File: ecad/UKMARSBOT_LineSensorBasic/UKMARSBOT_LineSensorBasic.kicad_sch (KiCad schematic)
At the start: 32 parts, among them J1 Conn_01x16, Q1 BC337-40, Q2 BPW85C, Q3 BPW85C, Q4 BPW85C, Q5 BPW85C, Q6 BC337-40

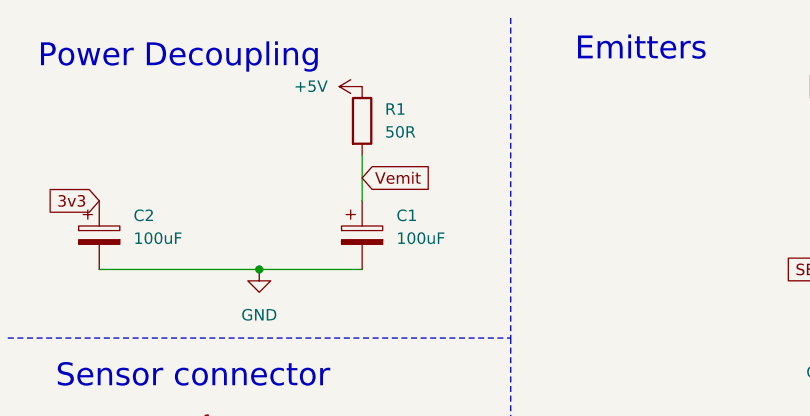
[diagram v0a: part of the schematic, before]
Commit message: Added RAPID field to all files and updated automation to pull this new field into BOM files
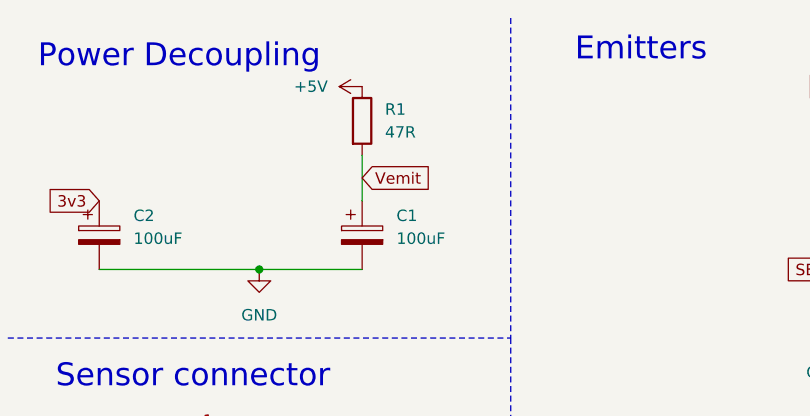
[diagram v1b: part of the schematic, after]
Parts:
- C1, C2: RAPID (none) -> 11-4109
- D1, D2, D7: RAPID (none) -> 55-0066
- D4: RAPID (none) -> 56-0400
- D5: RAPID (none) -> 56-0405
- D6: RAPID (none) -> 56-0410
- J1: RAPID (none) -> 19-0087
- Q1, Q6: RAPID (none) -> 50-3113
- R1: value 50R -> 47R; RAPID (none) -> 62-0334; RSONLINE (none) -> 707-8817
- R10, R11, R12, R14, R7, R8, R9: RAPID (none) -> 64-0068
- R15, R2: RAPID (none) -> 62-0360
- R16, R4: RAPID (none) -> 62-0394
- R17, R3, R5: RAPID (none) -> 62-0326

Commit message: V2.1 Boards ready for fabrication
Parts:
- C1, C2: footprint Capacitor_THT:CP_Radial_D5.0mm_P2.50mm -> Capacitor_THT:CP_Radial_D6.3mm_P2.50mm; RSONLINE 739-6799 -> 176-3779
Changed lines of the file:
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@@
 			)
 		)
-		(property "Footprint" "Capacitor_THT:CP_Radial_D5.0mm_P2.50mm"
+		(property "Footprint" "Capacitor_THT:CP_Radial_D6.3mm_P2.50mm"
 			(at 53.0352 41.91 0)
 			(effects
@@
 			)
 		)
-		(property "RSONLINE" "739-6799 "
+		(property "RSONLINE" "176-3779"
+			(at 52.07 38.1 0)
+			(effects
+				(font
+					(size 1.27 1.27)
+				)
+				(hide yes)
+			)
+		)
+		(property "RAPID" "11-4109"
 			(at 52.07 38.1 0)
 			(effects
@@
 			)
 		)
-		(property "Footprint" "Capacitor_THT:CP_Radial_D5.0mm_P2.50mm"
+		(property "Footprint" "Capacitor_THT:CP_Radial_D6.3mm_P2.50mm"
 			(at 23.8252 41.91 0)
 			(effects
@@
 			)
 		)
-		(property "RSONLINE" "739-6799 "
+		(property "RSONLINE" "176-3779 "
 			(at 22.86 38.1 0)
 			(effects
+				(font
+					(size 1.27 1.27)
+				)
+				(hide yes)
+			)
+		)
+		(property "RAPID" "11-4109"
+			(at 22.86 38.1 0)
+			(effects
